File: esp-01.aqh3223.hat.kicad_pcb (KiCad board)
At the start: 2 copper layers, 49.8 x 49.8 mm, 17 parts, among them J1 AC Terminal, J2 GPIO/I2C, Q1 BC547, Q2 BC547, SW1 VCC_Switch, U1 ESP-01v090, U2 AMS1117-3.3, U3 AQH3223, U4 AQH3223

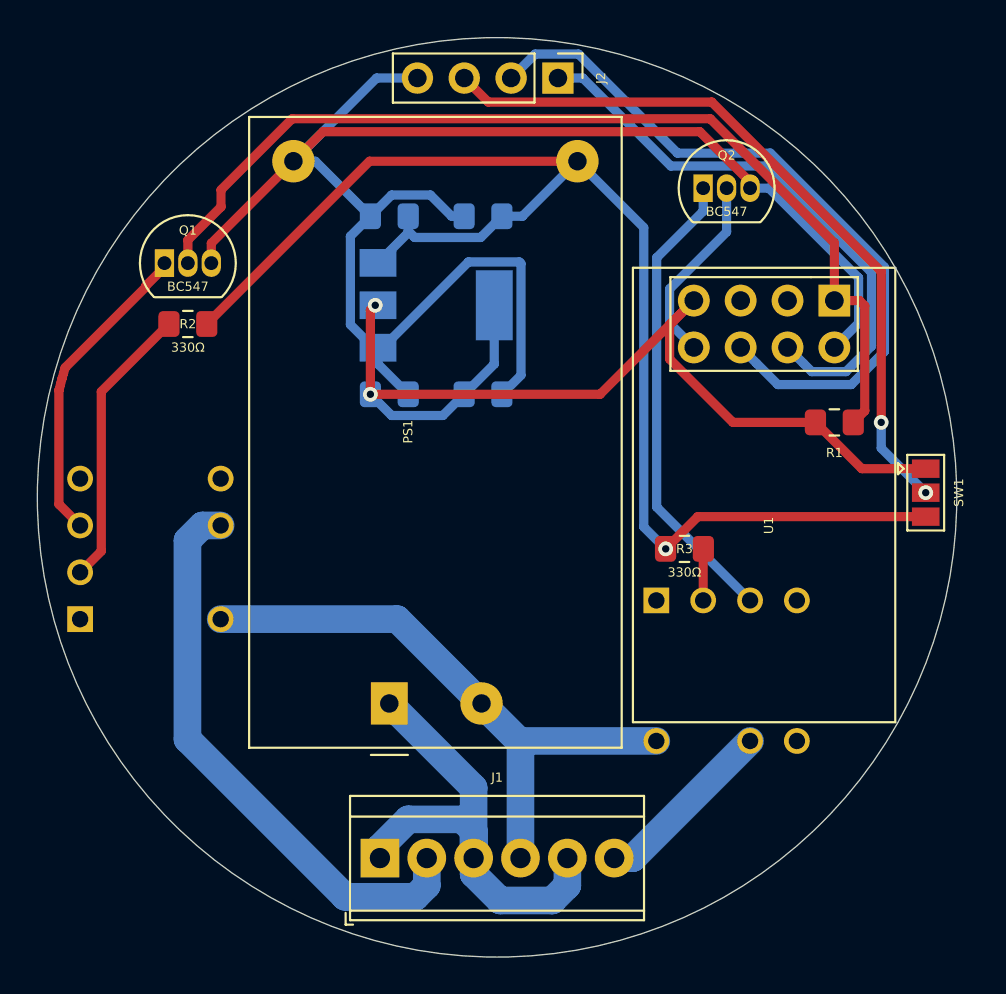
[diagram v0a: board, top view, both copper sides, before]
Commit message: fixed booting of esp-01
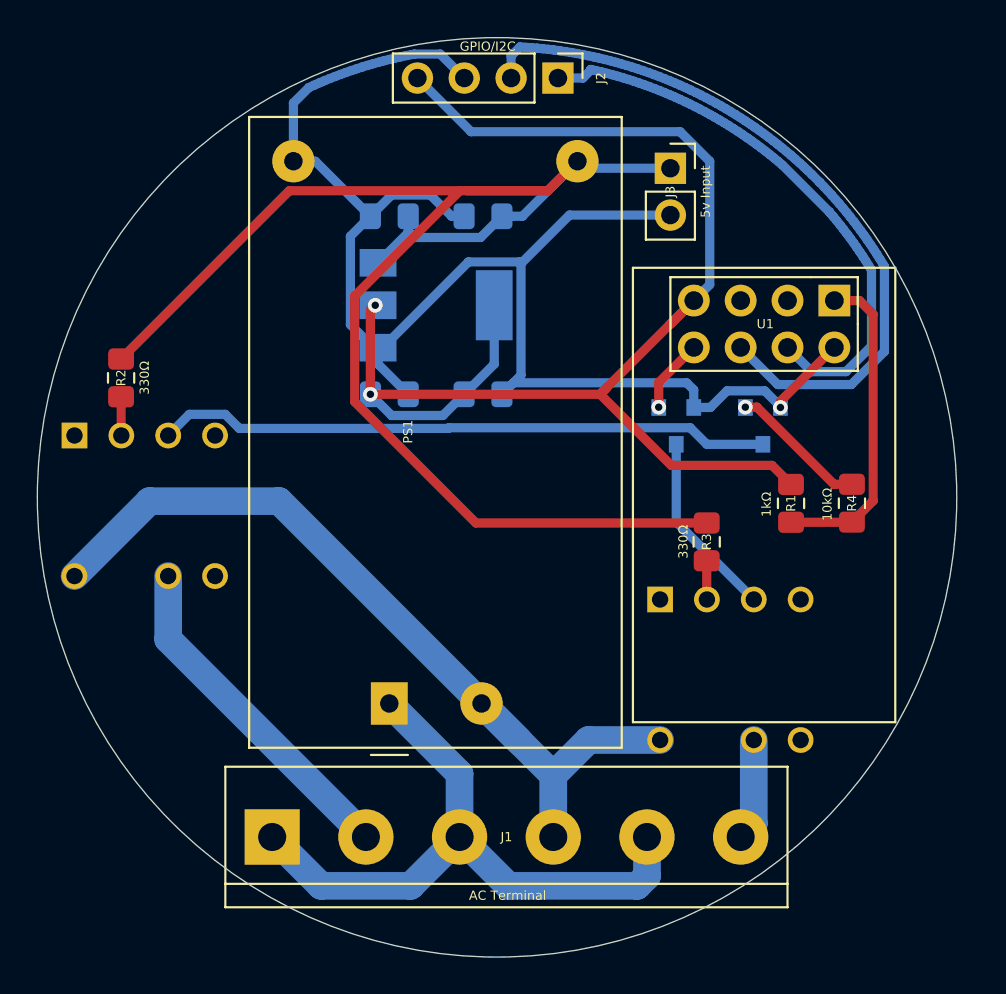
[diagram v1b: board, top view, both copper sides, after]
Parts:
- removed SW1: VCC_Switch, Jumper:SolderJumper-3_P1.3mm_Open_Pad1.0x1.5mm
- added J3: 5v Input, Connector_PinSocket_2.54mm:PinSocket_1x02_P2.54mm_Vertical, F.Cu at (161.8, 81.5)
- added R4: 10kΩ, Resistor_SMD:R_0805_2012Metric_Pad1.15x1.40mm_HandSolder, F.Cu at (171.6, 99.6)
- J1: footprint TerminalBlock_TE-Connectivity:TerminalBlock_TE_282834-6_1x06_P2.54mm_Horizontal -> TerminalBlock:TerminalBlock_bornier-6_P5.08mm
- Q1, Q2: value BC547 -> BC847; footprint Package_TO_SOT_THT:TO-92_Inline -> Package_TO_SOT_SMD:SOT-23; moved to B.Cu
- R1: value 4k7Ω -> 1kΩ
- moved Q1 33.6 mm to (166.8, 95.4), turned to 270 degrees
- moved Q2 13.0 mm to (162.1, 95.4), turned to 270 degrees
- moved U3 9.96 mm to (129.5, 96.0), turned to 270 degrees
- moved J1 5.95 mm to (140.2, 117.7)
- moved R1 4.98 mm to (168.3, 99.6), turned to 90 degrees
- moved R2 4.65 mm to (132.0, 92.8), turned to 90 degrees
- moved R3 1.27 mm to (163.8, 101.7), turned to 90 degrees
- moved U4 0.21 mm to (161.2, 104.9)
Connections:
- J2 pad 3: /I2C-VCC -> GND
- J2 pad 4: GND -> +3.3V
- Q1 pad 1: /TX-Relay -> Net-(Q1-Pad1)
- Q1 pad 2: /TX-Transistor -> GND
- Q1 pad 3: GND -> /TX-Relay
- Q2 pad 1: /RX-Relay -> /RX-Transistor
- Q2 pad 2: /RX-Transistor -> GND
- Q2 pad 3: GND -> /RX-Relay
- R1 pad 1: /TX-Transistor -> Net-(R1-Pad1)
- U1 pad 1: /TX-Transistor -> Net-(R1-Pad1)
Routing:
- net /TX-Transistor: track 53.8 -> 0.00 mm
- net /I2C-VCC: track 39.9 -> 0.00 mm, vias 2 -> 0
- net +3.3V: track 56.2 -> 76.5 mm
- net Net-(R1-Pad1): track 0.00 -> 17.5 mm
- net /TX-Relay: track 17.0 -> 33.4 mm
- net /RX-Relay: track 25.5 -> 10.2 mm
- net Earth: track 35.6 -> 49.6 mm
- net Net-(R2-Pad1): track 15.5 -> 2.10 mm
- net +5V: track 75.7 -> 88.7 mm, vias 1 -> 0
- net Relay1: track 31.2 -> 18.6 mm
- net GND: track 95.3 -> 84.7 mm, vias 0 -> 1
- net AC: track 26.7 -> 34.8 mm
- net Net-(Q1-Pad1): track 0.00 -> 7.51 mm, vias 0 -> 1
- net /RX-Transistor: track 10.5 -> 4.03 mm, vias 0 -> 1
- net Relay2: track 10.00 -> 6.27 mm
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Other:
- net class AC: clearance 0.3 -> 0.4
